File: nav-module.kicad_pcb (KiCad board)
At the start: 4 copper layers, 100 x 100 mm, 203 parts, among them J200 09031967921, J400 Conn_Coaxial, J800 USB_C_Receptacle_USB2.0_16P, Q700 MMST3904, SW400 TL2243, U100 W25Q128, U200 PESD5V0S2BT, U300 TPS563201DDCR, U301 TPS563201DDCR, U302 CH334P, U400 STM32H750VBTx, U401 ZED-F9P, U402 BNO055, U500 TJA1044GTK_3Z, U600 TJA1044GTK_3Z, U700 STM32F103CBTx, U801 FSUSB42UMX, U802 PESD5V0S2BT, X300 Q13FC1350000400, X400 X322512MSB4SI, X401 Q13FC1350000400, Y700 8 MHz, Y900 12Mhz

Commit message: [RF gps] update rev 1.1 fixed  update  rf place
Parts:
- moved kibuzzard-67B624A4 2.42 mm to (130.5, 119.6)
- moved kibuzzard-67B62451 2.38 mm to (128.1, 119.6)
- moved TP703 0.20 mm to (129.5, 120.6)
- moved TP702 0.19 mm to (127.1, 120.6)
- moved kibuzzard-67B62521 0.15 mm to (133.0, 119.7)
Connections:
- net Net-(C419-Pad2) renamed /GPS-RTK/RF_
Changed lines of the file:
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@@
 	(net 247 "unconnected-(U401-Reserved-Pad16)")
 	(net 248 "/GPS-RTK/NRST")
-	(net 249 "Net-(C419-Pad2)")
+	(net 249 "/GPS-RTK/RF_")
 	(net 250 "/GPS-RTK/RF_IN")
 	(net 251 "/GPS-RTK/VCC_RF")
@@
 			(layers "F.Cu" "F.Paste" "F.Mask")
 			(roundrect_rratio 0.25)
-			(net 249 "Net-(C419-Pad2)")
+			(net 249 "/GPS-RTK/RF_")
 			(pinfunction "2")
 			(pintype "passive")
@@
 			(layers "F.Cu" "F.Paste" "F.Mask")
 			(roundrect_rratio 0.25)
-			(net 249 "Net-(C419-Pad2)")
+			(net 249 "/GPS-RTK/RF_")
 			(pintype "passive")
 		)
@@
 			(layers "F.Cu" "F.Paste" "F.Mask")
 			(roundrect_rratio 0.25)
-			(net 249 "Net-(C419-Pad2)")
+			(net 249 "/GPS-RTK/RF_")
 			(pintype "passive")
 		)
@@
 	(footprint "kibuzzard-67B624A4"
 		(layer "B.Cu")
-		(at 128.09018 119.790403 45)
+		(at 130.5 119.575001 45)
 		(descr "Generated with KiBuzzard")
 		(tags "kb_params=eyJBbGlnbm1lbnRDaG9pY2UiOiAiQ2VudGVyIiwgIkNhcExlZnRDaG9pY2UiOiAiKCIsICJDYXBSaWdodENob2ljZSI6ICIpIiwgIkZvbnRDb21ib0JveCI6ICJVYnVudHVNb25vLUIiLCAiSGVpZ2h0Q3RybCI6IDAuOCwgIkxheWVyQ29tYm9Cb3giOiAiRi5TaWxrUyIsICJMaW5lU3BhY2luZ0N0cmwiOiAxLjUsICJNdWx0aUxpbmVUZXh0IjogIkJUMCIsICJQYWRkaW5nQm90dG9tQ3RybCI6IDMuMCwgIlBhZGRpbmdMZWZ0Q3RybCI6IDguNSwgIlBhZGRpbmdSaWdodEN0cmwiOiAwLjAsICJQYWRkaW5nVG9wQ3RybCI6IDMuMCwgIldpZHRoQ3RybCI6IDAuMCwgImFkdmFuY2VkQ2hlY2tib3giOiB0cnVlLCAiaW5saW5lRm9ybWF0VGV4dGJveCI6IGZhbHNlLCAibGluZW92ZXJTdHlsZUNob2ljZSI6ICJTcXVhcmUiLCAibGluZW92ZXJUaGlja25lc3NDdHJsIjogMX0=")
@@
 	(footprint "kibuzzard-67B62521"
 		(layer "B.Cu")
-		(at 132.97 119.839801 45)
+		(at 132.97 119.685001 45)
 		(descr "Generated with KiBuzzard")
 		(tags "kb_params=eyJBbGlnbm1lbnRDaG9pY2UiOiAiQ2VudGVyIiwgIkNhcExlZnRDaG9pY2UiOiAiKCIsICJDYXBSaWdodENob2ljZSI6ICIpIiwgIkZvbnRDb21ib0JveCI6ICJVYnVudHVNb25vLUIiLCAiSGVpZ2h0Q3RybCI6IDAuOCwgIkxheWVyQ29tYm9Cb3giOiAiRi5TaWxrUyIsICJMaW5lU3BhY2luZ0N0cmwiOiAxLjUsICJNdWx0aUxpbmVUZXh0IjogIk4vQyIsICJQYWRkaW5nQm90dG9tQ3RybCI6IDMuMCwgIlBhZGRpbmdMZWZ0Q3RybCI6IDguNSwgIlBhZGRpbmdSaWdodEN0cmwiOiAwLjAsICJQYWRkaW5nVG9wQ3RybCI6IDMuMCwgIldpZHRoQ3RybCI6IDAuMCwgImFkdmFuY2VkQ2hlY2tib3giOiB0cnVlLCAiaW5saW5lRm9ybWF0VGV4dGJveCI6IGZhbHNlLCAibGluZW92ZXJTdHlsZUNob2ljZSI6ICJTcXVhcmUiLCAibGluZW92ZXJUaGlja25lc3NDdHJsIjogMX0=")
@@
 	(footprint "TestPoint:TestPoint_Pad_D1.0mm"
 		(layer "B.Cu")
-		(at 129.5 120.775)
+		(at 129.5 120.575001)
 		(descr "SMD pad as test Point, diameter 1.0mm")
 		(tags "test point SMD pad")
@@
 	(footprint "kibuzzard-67B62451"
 		(layer "B.Cu")
-		(at 130.445194 119.809144 45)
+		(at 128.08 119.585001 45)
 		(descr "Generated with KiBuzzard")
 		(tags "kb_params=eyJBbGlnbm1lbnRDaG9pY2UiOiAiQ2VudGVyIiwgIkNhcExlZnRDaG9pY2UiOiAiKCIsICJDYXBSaWdodENob2ljZSI6ICIpIiwgIkZvbnRDb21ib0JveCI6ICJVYnVudHVNb25vLUIiLCAiSGVpZ2h0Q3RybCI6IDAuOCwgIkxheWVyQ29tYm9Cb3giOiAiRi5TaWxrUyIsICJMaW5lU3BhY2luZ0N0cmwiOiAxLjUsICJNdWx0aUxpbmVUZXh0IjogIjNWMyIsICJQYWRkaW5nQm90dG9tQ3RybCI6IDMuMCwgIlBhZGRpbmdMZWZ0Q3RybCI6IDguNSwgIlBhZGRpbmdSaWdodEN0cmwiOiAwLjAsICJQYWRkaW5nVG9wQ3RybCI6IDMuMCwgIldpZHRoQ3RybCI6IDAuMCwgImFkdmFuY2VkQ2hlY2tib3giOiB0cnVlLCAiaW5saW5lRm9ybWF0VGV4dGJveCI6IGZhbHNlLCAibGluZW92ZXJTdHlsZUNob2ljZSI6ICJTcXVhcmUiLCAibGluZW92ZXJUaGlja25lc3NDdHJsIjogMX0=")
@@
 	(footprint "TestPoint:TestPoint_Pad_D1.0mm"
 		(layer "B.Cu")
-		(at 127.1 120.775)
+		(at 127.1 120.585001)
 		(descr "SMD pad as test Point, diameter 1.0mm")
 		(tags "test point SMD pad")
@@
 	)
 	(segment
+		(start 127.1 120.775)
+		(end 127.1 120.585001)
+		(width 0.3)
+		(layer "B.Cu")
+		(net 1)
+	)
+	(segment
 		(start 127.9 121.575)
 		(end 127.1 120.775)
@@
 	)
 	(via
-		(at 70.255816 61.100817)
+		(at 70.31 60.995001)
 		(size 0.5)
 		(drill 0.3)
@@
 	)
 	(via
-		(at 69.37 61.085001)
+		(at 69.54 61.025001)
 		(size 0.5)
 		(drill 0.3)
@@
 	)
 	(segment
-		(start 130.275 120.775)
+		(start 130.075001 120.575001)
 		(end 130.675 121.175)
 		(width 0.2)
@@
 	)
 	(segment
-		(start 129.5 120.775)
-		(end 130.275 120.775)
+		(start 129.5 120.575001)
+		(end 130.075001 120.575001)
 		(width 0.2)
 		(layer "B.Cu")
@@
 	)
 	(segment
-		(start 65.829998 62.135001)
-		(end 70.305 62.135001)
-		(width 0.45)
+		(start 65.84 63.005002)
+		(end 65.84 62.485001)
+		(width 0.4)
 		(layer "F.Cu")
 		(net 249)
 	)
 	(segment
-		(start 70.305 62.135001)
-		(end 70.325 62.155001)
-		(width 0.45)
+		(start 65.84 62.485001)
+		(end 66.17 62.155001)
+		(width 0.4)
 		(layer "F.Cu")
 		(net 249)
 	)
 	(segment
-		(start 65.829998 62.135001)
-		(end 65.829998 62.995)
-		(width 0.45)
+		(start 66.17 62.155001)
+		(end 70.32 62.155001)
+		(width 0.4)
 		(layer "F.Cu")
 		(net 249)
 	)
 	(segment
-		(start 65.829998 62.995)
-		(end 65.84 63.005002)
-		(width 0.45)
+		(start 71.33 65.925002)
+		(end 71.33 56.035001)
+		(width 0.4)
 		(layer "F.Cu")
-		(net 249)
+		(net 250)
 	)
 	(segment
 		(start 71.33 56.035001)
 		(end 71.35 56.015001)
-		(width 0.6)
-		(layer "F.Cu")
-		(net 250)
-	)
-	(segment
-		(start 71.33 65.925002)
-		(end 71.33 56.035001)
-		(width 0.6)
+		(width 0.4)
 		(layer "F.Cu")
 		(net 250)
 	)
 	(segment
-		(start 65.83 64.015)
-		(end 65.84 64.005)
-		(width 0.6)
+		(start 65.83 64.025002)
+		(end 65.89 63.965002)
+		(width 0.4)
 		(layer "F.Cu")
 		(net 251)
@@
 	(segment
 		(start 65.83 65.925002)
-		(end 65.83 64.015)
-		(width 0.6)
+		(end 65.83 64.025002)
+		(width 0.4)
 		(layer "F.Cu")
 		(net 251)

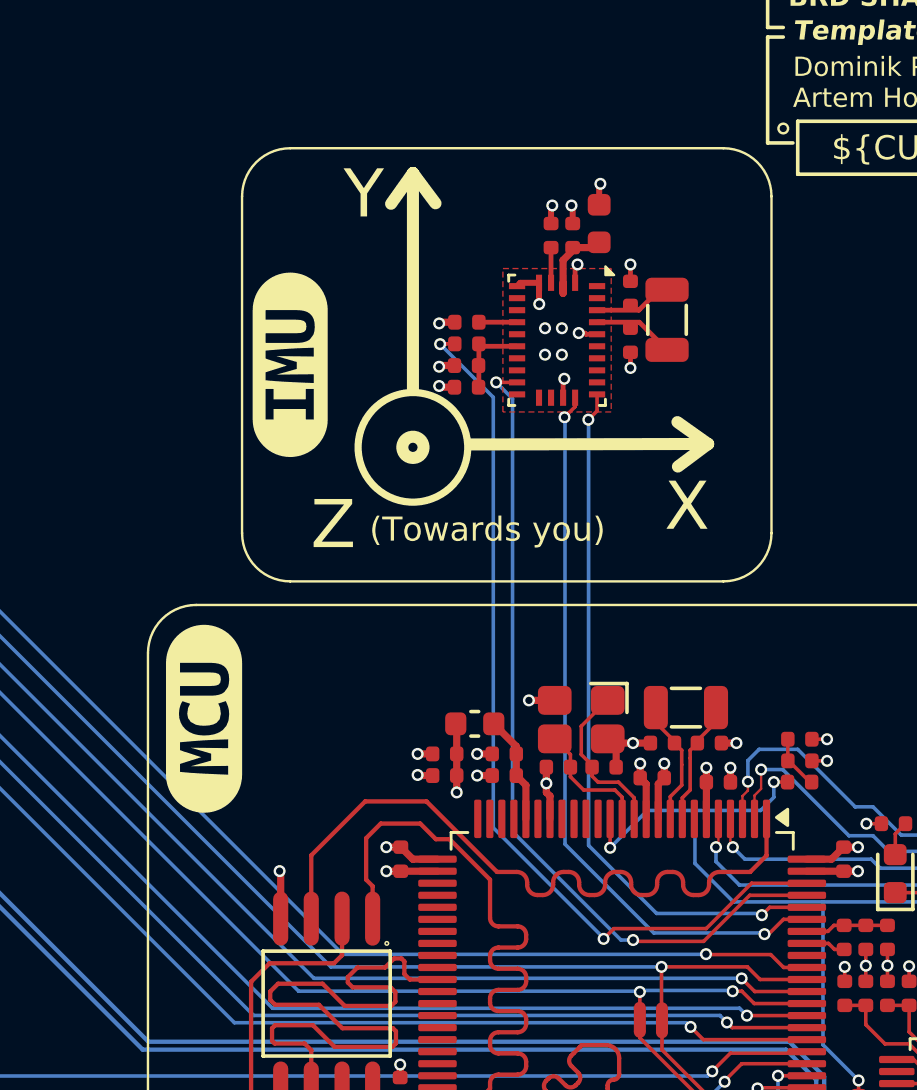
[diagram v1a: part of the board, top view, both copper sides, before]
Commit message: [3d models] added 3d models for gps and can tranciver
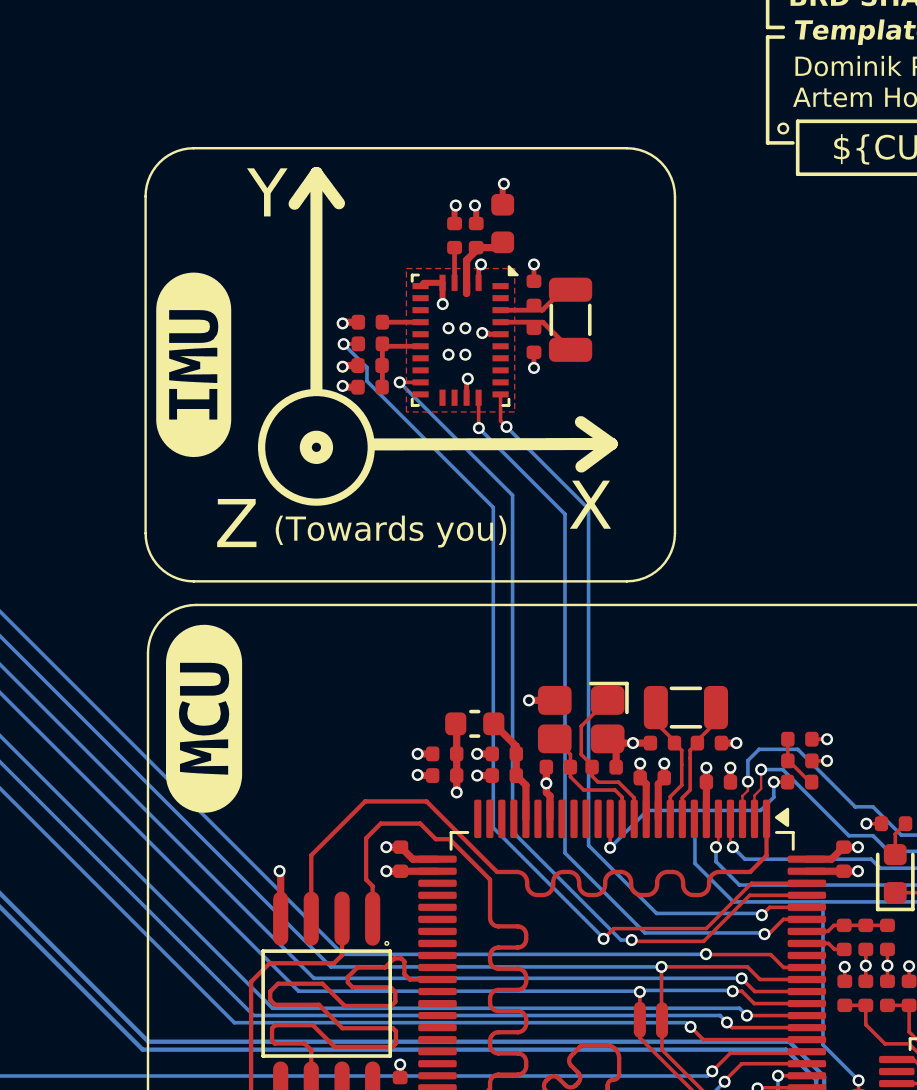
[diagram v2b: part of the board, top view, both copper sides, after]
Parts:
- moved C420 4.01 mm to (107.1, 84.4)
- moved C421 4.01 mm to (101.6, 91.2)
- moved C425 4.01 mm to (101.6, 88.5)
- moved R419 4.01 mm to (101.6, 89.4)
- moved R420 4.01 mm to (101.6, 90.3)
- moved R421 4.01 mm to (105.1, 84.9)
- moved U402 4.01 mm to (105.4, 89.3)
- moved kibuzzard-67B69E78 4.01 mm to (94.3, 90.3)
- moved C422 4.01 mm to (106.0, 84.9)
- moved C423 4.01 mm to (108.4, 89.3)
- moved C424 4.01 mm to (108.4, 87.3)
- moved X401 4.01 mm to (109.9, 88.4)
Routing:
- net /IMU/IMU_EXINTERUPT: track 34.7 -> 36.4 mm
- net /IMU/IMU_NRESET: track 37.5 -> 39.2 mm
- net /IMU/IMU_I2C.SCL: track 30.6 -> 32.1 mm
- net /IMU/IMU_I2C.SDA: track 29.3 -> 30.7 mm

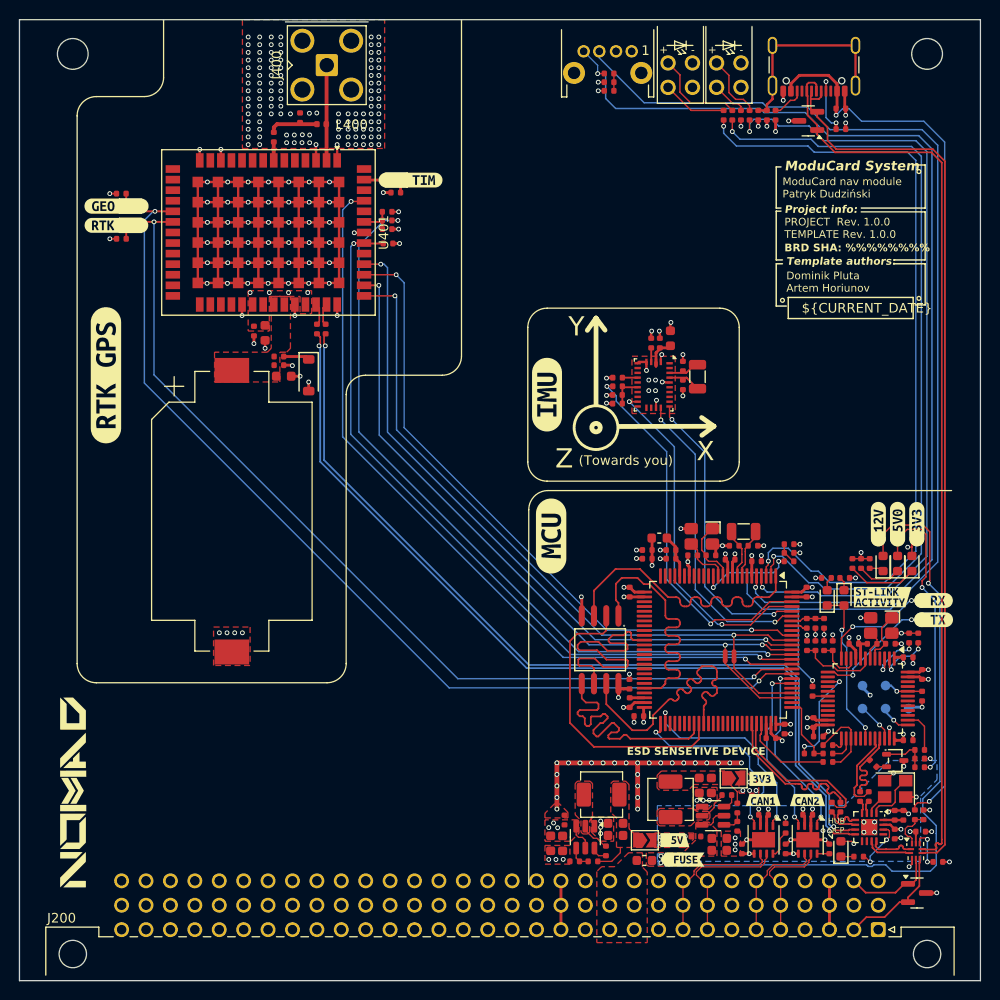
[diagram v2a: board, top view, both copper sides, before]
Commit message: final check , added pull up resistors on i2c
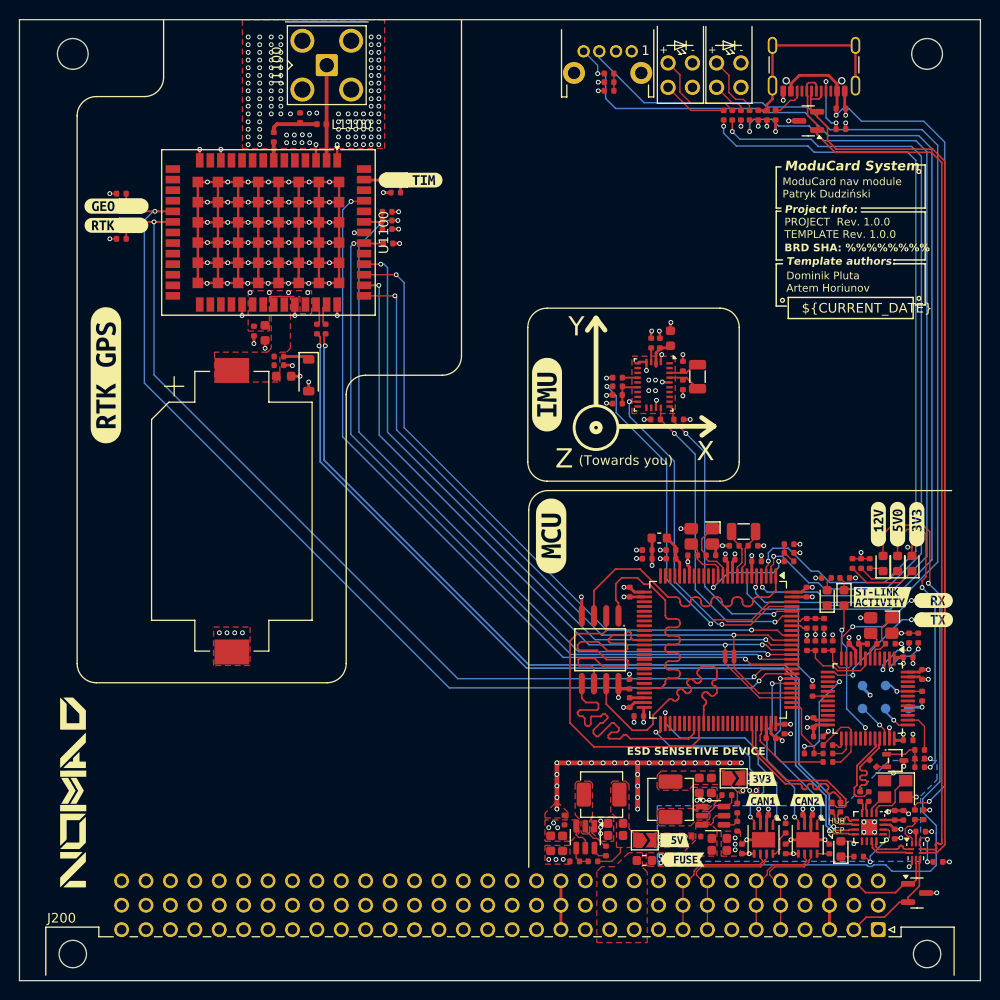
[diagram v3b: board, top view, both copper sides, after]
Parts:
- added R426: 4.7kΩ, PCM_JLCPCB:R_0402, F.Cu at (105.6, 92.9)
- added R427: 4.7kΩ, PCM_JLCPCB:R_0402, F.Cu at (108.0, 92.9)
- renumbered BAT400 to BAT1100, C1117 to C1100, C417 to C1101, C426 to C1102, C427 to C1103, C419 to C1104, C418 to C1105, C420 to C1200, C422 to C1201, C423 to C1202, C424 to C1203, C421 to C1204, C425 to C1205, D408 to D1100, D404 to D1101, D403 to D1102, D405 to D1103, J400 to J1100, L400 to L1100, NT400 to NT1100, NT401 to NT1101, R425 to R1100, R413 to R1101, R415 to R1102, R414 to R1103, R417 to R1104, R423 to R1105, R422 to R1106, R424 to R1107, R421 to R1200, R420 to R1201, R419 to R1202, U401 to U1100, U402 to U1200, X401 to X1200
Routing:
- net +3V3: track 51.0 -> 52.4 mm, vias 42 -> 44
- net GND: vias 286 -> 285

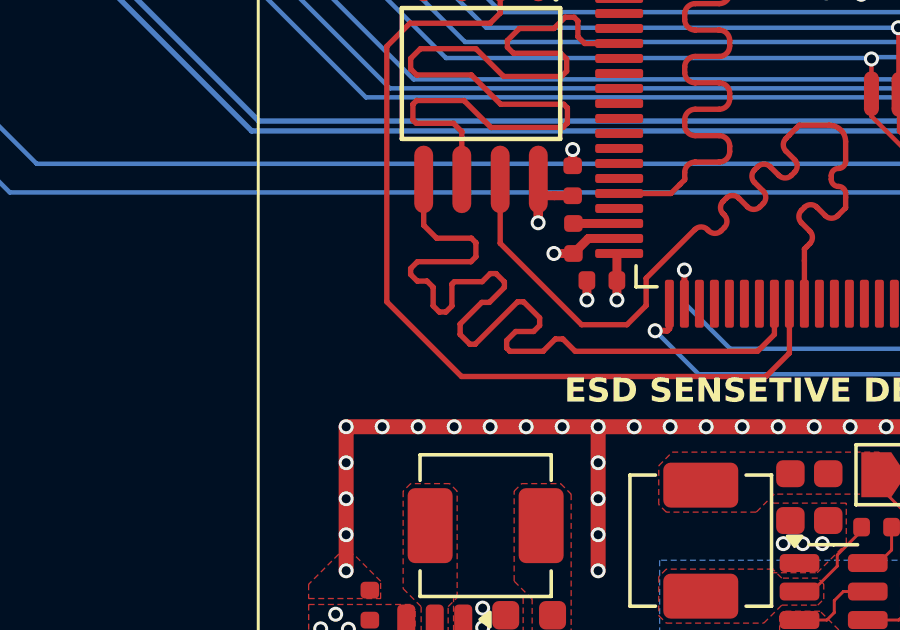
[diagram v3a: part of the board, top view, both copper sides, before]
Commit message: added icons on silkscreen
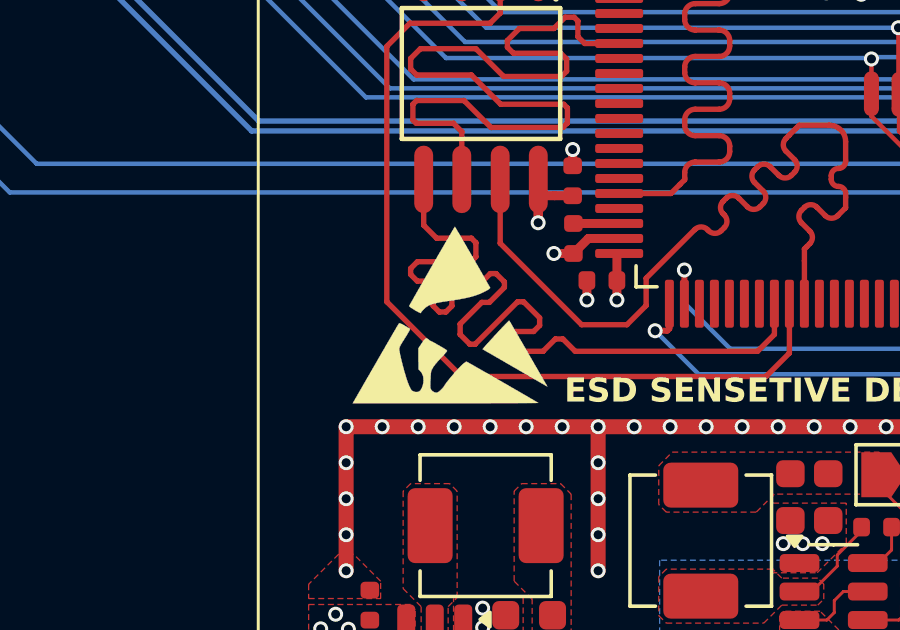
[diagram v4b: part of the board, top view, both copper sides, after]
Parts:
- added REF**: ESD-Logo_6.6x6mm_SilkScreen, Symbol:ESD-Logo_6.6x6mm_SilkScreen, F.Cu at (98.8, 124.9)
- added REF**: OSHW-Symbol_6.7x6mm_SilkScreen, Symbol:OSHW-Symbol_6.7x6mm_SilkScreen, B.Cu at (116.6, 117.1)
